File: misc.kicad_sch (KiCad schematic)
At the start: 35 parts, among them J2 Tag-Connect_TC2030-IDC-NL_2x3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, U1 MPFS250T-FCVG484, U2 SDINBDG4-8G, U3 MT25QL01GBBB1EW9-0SIT

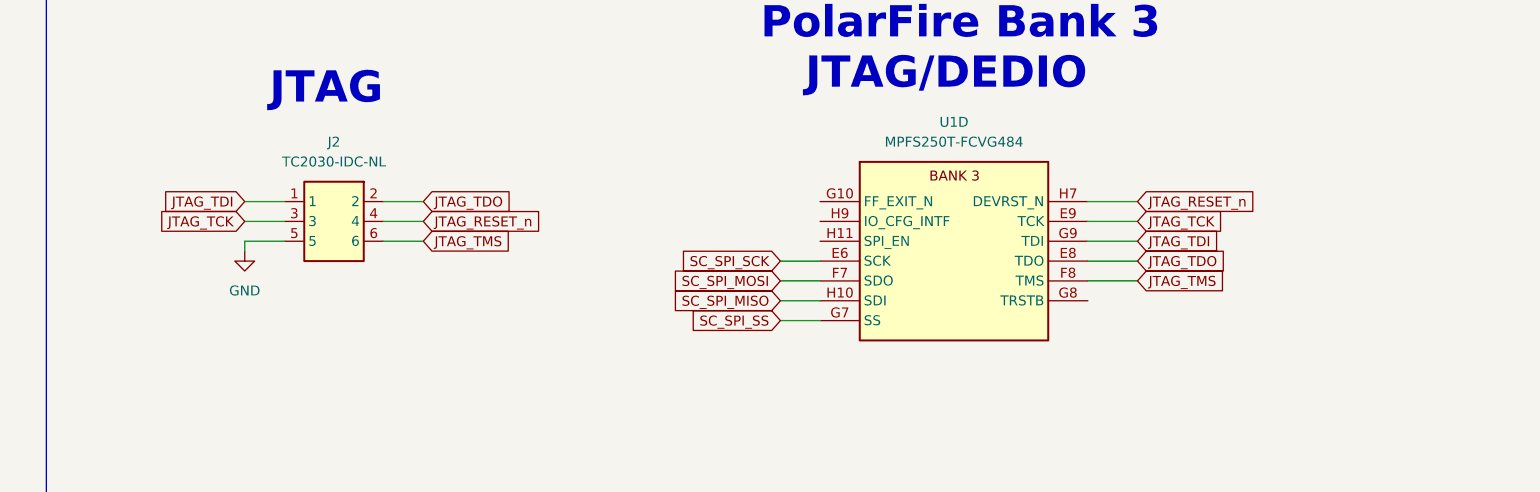
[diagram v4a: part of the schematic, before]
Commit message: [#54178] Add JTAG chain, rename WiFi subsheet
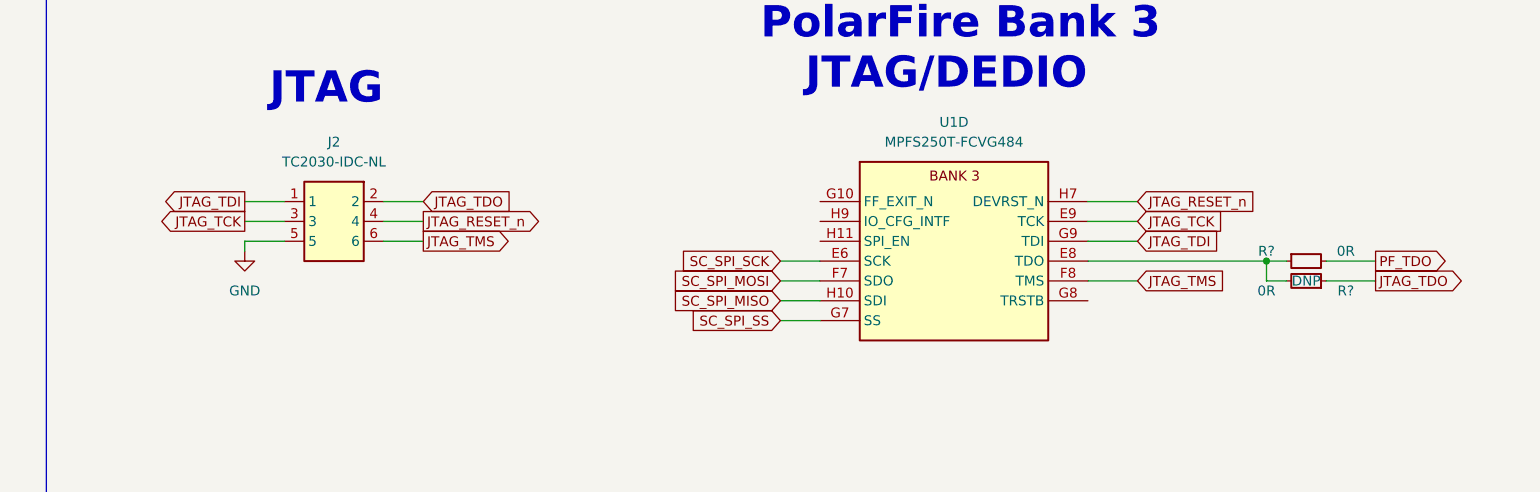
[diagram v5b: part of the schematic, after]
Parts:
- added R? (x2): R_0R_0402, antmicro-footprints:R_0402_1005Metric, symbol antmicroResistors0402:R_0R_0402
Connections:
- net JTAG_TDO: now also R?.1; no longer U1.E8 (TDO)
- new net: R?.1, R?.2, U1.E8 (TDO)
- new net PF_TDO: R?.2
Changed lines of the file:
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@@
   (junction (at 184.15 208.28) (diameter 0) (color 0 0 0 0)
   )
+  (junction (at 374.65 82.55) (diameter 0) (color 0 0 0 0)
+  )
   (junction (at 172.72 208.28) (diameter 0) (color 0 0 0 0)
   )
@@
     (stroke (width 0) (type default) (color 0 0 0 0))
   )
+  (wire (pts (xy 382.27 85.09) (xy 388.62 85.09))
+    (stroke (width 0) (type default) (color 0 0 0 0))
+  )
   (wire (pts (xy 83.82 71.12) (xy 86.36 71.12))
     (stroke (width 0) (type default) (color 0 0 0 0))
@@
     (stroke (width 0) (type default) (color 0 0 0 0))
   )
+  (wire (pts (xy 374.65 85.09) (xy 374.65 82.55))
+    (stroke (width 0) (type default) (color 0 0 0 0))
+  )
   (wire (pts (xy 374.65 186.69) (xy 379.73 186.69))
     (stroke (width 0) (type default) (color 0 0 0 0))
@@
     (stroke (width 0) (type default) (color 0 0 0 0))
   )
+  (wire (pts (xy 377.19 85.09) (xy 374.65 85.09))
+    (stroke (width 0) (type default) (color 0 0 0 0))
+  )
   (wire (pts (xy 172.72 219.71) (xy 168.91 219.71))
     (stroke (width 0) (type default) (color 0 0 0 0))
@@
     (stroke (width 0) (type default) (color 0 0 0 0))
   )
-  (wire (pts (xy 351.79 82.55) (xy 358.14 82.55))
+  (wire (pts (xy 351.79 82.55) (xy 374.65 82.55))
     (stroke (width 0) (type default) (color 0 0 0 0))
   )
@@
     (stroke (width 0) (type default) (color 0 0 0 0))
   )
+  (wire (pts (xy 382.27 82.55) (xy 388.62 82.55))
+    (stroke (width 0) (type default) (color 0 0 0 0))
+  )
   (wire (pts (xy 148.59 73.66) (xy 151.13 73.66))
     (stroke (width 0) (type default) (color 0 0 0 0))
@@
     (stroke (width 0) (type default) (color 0 0 0 0))
   )
+  (wire (pts (xy 374.65 82.55) (xy 377.19 82.55))
+    (stroke (width 0) (type default) (color 0 0 0 0))
+  )
   (wire (pts (xy 256.54 173.99) (xy 256.54 179.07))
     (stroke (width 0) (type default) (color 0 0 0 0))
@@
     )
   )
-  (global_label "JTAG_TMS" (shape input) (at 266.7 80.01 0) (fields_autoplaced)
+  (global_label "JTAG_TMS" (shape output) (at 266.7 80.01 0) (fields_autoplaced)
     (effects (font (size 1.27 1.27)) (justify left))
     (property "Intersheet References" "${INTERSHEET_REFS}" (id 0) (at 278.0031 79.9306 0)
@@
     )
   )
-  (global_label "JTAG_TDI" (shape input) (at 243.84 74.93 180) (fields_autoplaced)
+  (global_label "JTAG_TDI" (shape output) (at 243.84 74.93 180) (fields_autoplaced)
     (effects (font (size 1.27 1.27)) (justify right))
-    (property "Intersheet References" "${INTERSHEET_REFS}" (id 0) (at 233.3231 75.0094 0)
+    (property "Intersheet References" "${INTERSHEET_REFS}" (id 0) (at 233.3231 74.8506 0)
       (effects (font (size 1.27 1.27)) (justify right) hide)
     )
@@
     )
   )
-  (global_label "JTAG_TCK" (shape input) (at 243.84 77.47 180) (fields_autoplaced)
+  (global_label "JTAG_TCK" (shape output) (at 243.84 77.47 180) (fields_autoplaced)
     (effects (font (size 1.27 1.27)) (justify right))
-    (property "Intersheet References" "${INTERSHEET_REFS}" (id 0) (at 232.6579 77.5494 0)
+    (property "Intersheet References" "${INTERSHEET_REFS}" (id 0) (at 232.6579 77.3906 0)
       (effects (font (size 1.27 1.27)) (justify right) hide)
     )
   )
+  (global_label "JTAG_TDO" (shape output) (at 388.62 85.09 0) (fields_autoplaced)
+    (effects (font (size 1.27 1.27)) (justify left))
+    (property "Intersheet References" "${INTERSHEET_REFS}" (id 0) (at 399.8626 85.0106 0)
+      (effects (font (size 1.27 1.27)) (justify left) hide)
+    )
+  )
   (global_label "MEM_DAT3" (shape input) (at 48.26 210.82 180) (fields_autoplaced)
     (effects (font (size 1.27 1.27)) (justify right))
@@
     )
   )
-  (global_label "JTAG_TDO" (shape input) (at 358.14 82.55 0) (fields_autoplaced)
+  (global_label "PF_TDO" (shape output) (at 388.62 82.55 0) (fields_autoplaced)
     (effects (font (size 1.27 1.27)) (justify left))
-    (property "Intersheet References" "${INTERSHEET_REFS}" (id 0) (at 369.3826 82.4706 0)
+    (property "Intersheet References" "${INTERSHEET_REFS}" (id 0) (at 397.9274 82.4706 0)
       (effects (font (size 1.27 1.27)) (justify left) hide)
     )
@@
     )
   )
-  (global_label "JTAG_RESET_n" (shape input) (at 266.7 77.47 0) (fields_autoplaced)
+  (global_label "JTAG_RESET_n" (shape output) (at 266.7 77.47 0) (fields_autoplaced)
     (effects (font (size 1.27 1.27)) (justify left))
     (property "Intersheet References" "${INTERSHEET_REFS}" (id 0) (at 282.2364 77.3906 0)
@@
     (pin "2")
   )
+  (symbol (lib_id "antmicroResistors0402:R_0R_0402") (at 382.27 85.09 180) (unit 1)
+    (in_bom yes) (on_board yes)
+    (property "Reference" "R?" (id 0) (at 384.81 86.36 0)
+      (effects (font (size 1.27 1.27) (thickness 0.15)))
+    )
+    (property "Value" "R_0R_0402" (id 1) (at 361.95 72.39 0)
+      (effects (font (size 1.27 1.27) (thickness 0.15)) (justify left bottom) hide)
+    )
+    (property "Footprint" "antmicro-footprints:R_0402_1005Metric" (id 2) (at 361.95 69.85 0)
+      (effects (font (size 1.27 1.27) (thickness 0.15)) (justify left bottom) hide)
+    )
+    (property "Datasheet" "https://industrial.panasonic.com/cdbs/www-data/pdf/RDA0000/AOA0000C301.pdf" (id 3) (at 361.95 67.31 0)
+      (effects (font (size 1.27 1.27) (thickness 0.15)) (justify left bottom) hide)
+    )
+    (property "MPN" "ERJ2GE0R00X" (id 4) (at 361.95 64.77 0)
+      (effects (font (size 1.27 1.27) (thickness 0.15)) (justify left bottom) hide)
+    )
+    (property "Manufacturer" "Panasonic" (id 5) (at 361.95 62.23 0)
+      (effects (font (size 1.27 1.27) (thickness 0.15)) (justify left bottom) hide)
+    )
+    (property "License" "Apache-2.0" (id 6) (at 361.95 59.69 0)
+      (effects (font (size 1.27 1.27) (thickness 0.15)) (justify left bottom) hide)
+    )
+    (property "Author" "Antmicro" (id 7) (at 361.95 57.15 0)
+      (effects (font (size 1.27 1.27) (thickness 0.15)) (justify left bottom) hide)
+    )
+    (property "Val" "0R" (id 8) (at 374.65 86.36 0)
+      (effects (font (size 1.27 1.27) (thickness 0.15)))
+    )
+    (property "Tolerance" "~" (id 9) (at 361.95 74.93 0)
+      (effects (font (size 1.27 1.27)) (justify left bottom) hide)
+    )
+    (property "Current" "1A" (id 10) (at 361.95 54.61 0)
+      (effects (font (size 1.27 1.27) (thickness 0.15)) (justify left bottom) hide)
+    )
+    (property "DNP" "DNP" (id 11) (at 379.73 85.09 0))
+    (pin "1")
+    (pin "2")
+  )
   (symbol (lib_id "antmicroCapacitors0402:C_100n_25V_0402") (at 176.53 181.61 90) (mirror x) (unit 1)
     (in_bom yes) (on_board yes)
@@
     )
     (pin "1")
+    (pin "2")
+  )
+  (symbol (lib_id "antmicroResistors0402:R_0R_0402") (at 377.19 82.55 0) (unit 1)
+    (in_bom yes) (on_board yes)
+    (property "Reference" "R?" (id 0) (at 374.65 81.28 0)
+      (effects (font (size 1.27 1.27) (thickness 0.15)))
+    )
+    (property "Value" "R_0R_0402" (id 1) (at 397.51 95.25 0)
+      (effects (font (size 1.27 1.27) (thickness 0.15)) (justify left bottom) hide)
+    )
+    (property "Footprint" "antmicro-footprints:R_0402_1005Metric" (id 2) (at 397.51 97.79 0)
+      (effects (font (size 1.27 1.27) (thickness 0.15)) (justify left bottom) hide)
+    )
+    (property "Datasheet" "https://industrial.panasonic.com/cdbs/www-data/pdf/RDA0000/AOA0000C301.pdf" (id 3) (at 397.51 100.33 0)
+      (effects (font (size 1.27 1.27) (thickness 0.15)) (justify left bottom) hide)
+    )
+    (property "MPN" "ERJ2GE0R00X" (id 4) (at 397.51 102.87 0)
+      (effects (font (size 1.27 1.27) (thickness 0.15)) (justify left bottom) hide)
+    )
+    (property "Manufacturer" "Panasonic" (id 5) (at 397.51 105.41 0)
+      (effects (font (size 1.27 1.27) (thickness 0.15)) (justify left bottom) hide)
+    )
+    (property "License" "Apache-2.0" (id 6) (at 397.51 107.95 0)
+      (effects (font (size 1.27 1.27) (thickness 0.15)) (justify left bottom) hide)
+    )
+    (property "Author" "Antmicro" (id 7) (at 397.51 110.49 0)
+      (effects (font (size 1.27 1.27) (thickness 0.15)) (justify left bottom) hide)
+    )
+    (property "Val" "0R" (id 8) (at 384.81 81.28 0)
+      (effects (font (size 1.27 1.27) (thickness 0.15)))
+    )
+    (property "Tolerance" "~" (id 9) (at 397.51 92.71 0)
+      (effects (font (size 1.27 1.27)) (justify left bottom) hide)
+    )
+    (property "Current" "1A" (id 10) (at 397.51 113.03 0)
+      (effects (font (size 1.27 1.27) (thickness 0.15)) (justify left bottom) hide)
+    )
+    (pin "1")

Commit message: [#54491] Exclude DNP from BOM
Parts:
- R20, R21, R22, R?: now left out of the parts list
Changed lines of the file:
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@@
   )
   (symbol (lib_id "antmicroResistorNetworksArrays:R_4x0R_0201_array") (at 138.43 66.04 0) (unit 1)
-    (in_bom yes) (on_board yes)
+    (in_bom no) (on_board yes)
     (property "Reference" "R20" (id 0) (at 143.51 59.69 0)
       (effects (font (size 1.27 1.27) (thickness 0.15)))
@@
   )
   (symbol (lib_id "antmicroResistors0402:R_0R_0402") (at 382.27 85.09 180) (unit 1)
-    (in_bom yes) (on_board yes)
+    (in_bom no) (on_board yes)
     (property "Reference" "R?" (id 0) (at 384.81 86.36 0)
       (effects (font (size 1.27 1.27) (thickness 0.15)))
@@
   )
   (symbol (lib_id "antmicroResistors0402:R_0R_0402") (at 140.97 96.52 0) (unit 1)
-    (in_bom yes) (on_board yes)
+    (in_bom no) (on_board yes)
     (property "Reference" "R22" (id 0) (at 138.43 95.25 0)
       (effects (font (size 1.27 1.27) (thickness 0.15)))
@@
   )
   (symbol (lib_id "antmicroResistorNetworksArrays:R_4x0R_0201_array") (at 138.43 77.47 0) (unit 1)
-    (in_bom yes) (on_board yes)
+    (in_bom no) (on_board yes)
     (property "Reference" "R21" (id 0) (at 143.51 87.63 0)
       (effects (font (size 1.27 1.27) (thickness 0.15)))
@@
   (symbol (lib_id "antmicropower:GND") (at 195.58 190.5 0) (unit 1)
     (in_bom yes) (on_board yes) (fields_autoplaced)
-    (property "Reference" "#PWR?" (id 0) (at 204.47 193.04 0)
-      (effects (font (size 1.27 1.27) (thickness 0.15)) (justify left bottom) hide)
-    )
+    (property "Reference" "#PWR0161" (id 0) (at 204.47 193.04 0)
+      (effects (font (size 1.27 1.27) (thickness 0.15)) (justify left bottom) hide)
+    )

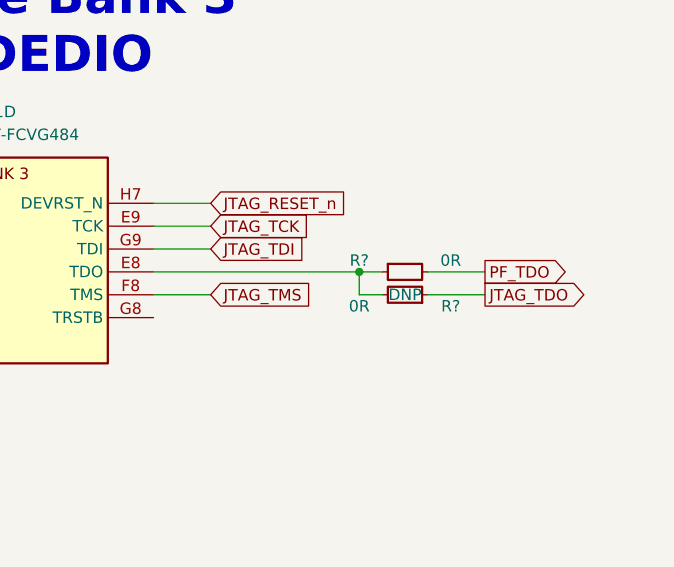
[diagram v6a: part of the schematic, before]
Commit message: [#54491] Annotate schematics
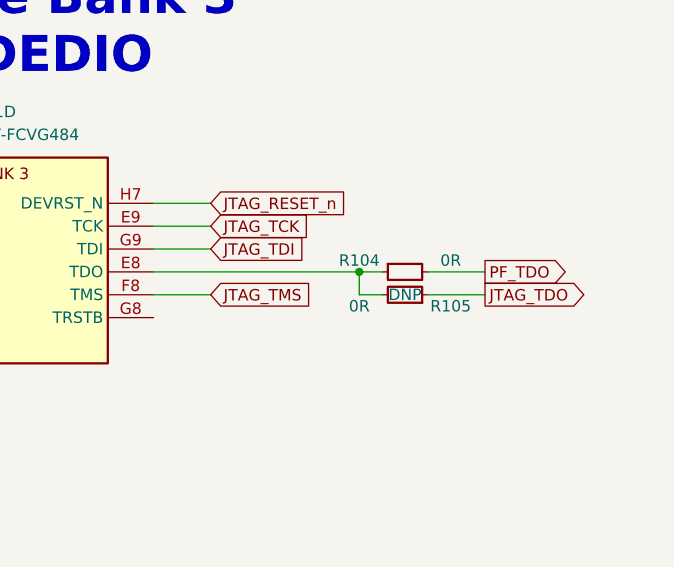
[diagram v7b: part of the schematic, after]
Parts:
- gave numbers to parts that had none: 2
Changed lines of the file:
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@@
   (symbol (lib_id "antmicroResistors0402:R_0R_0402") (at 382.27 85.09 180) (unit 1)
     (in_bom no) (on_board yes)
-    (property "Reference" "R?" (id 0) (at 384.81 86.36 0)
+    (property "Reference" "R105" (id 0) (at 384.81 86.36 0)
       (effects (font (size 1.27 1.27) (thickness 0.15)))
     )
@@
   (symbol (lib_id "antmicroResistors0402:R_0R_0402") (at 377.19 82.55 0) (unit 1)
     (in_bom yes) (on_board yes)
-    (property "Reference" "R?" (id 0) (at 374.65 81.28 0)
-      (effects (font (size 1.27 1.27) (thickness 0.15)))
-    )
+    (property "Reference" "R104" (id 0) (at 374.65 81.28 0)
+      (effects (font (size 1.27 1.27) (thickness 0.15)))
+    )
